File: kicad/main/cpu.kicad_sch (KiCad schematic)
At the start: 13 parts, among them SW1 SW_Push, U1 MC68030RC_PGA, U2 74HC74, U7 CY62256-70PC, Y1 CXO_DIP8

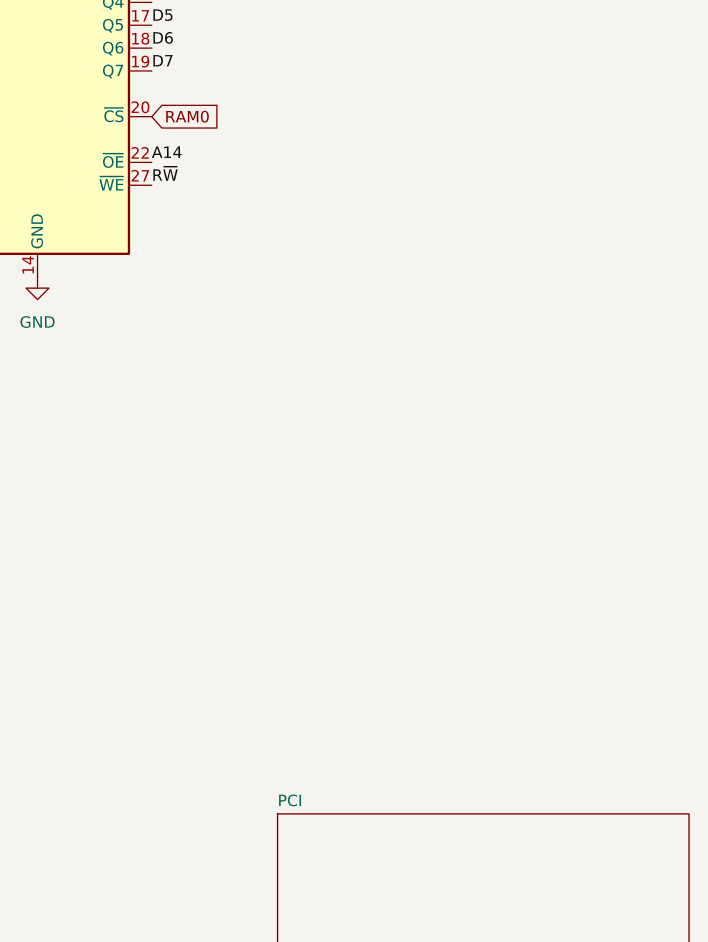
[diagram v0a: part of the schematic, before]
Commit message: rename az030 unix to az/ux
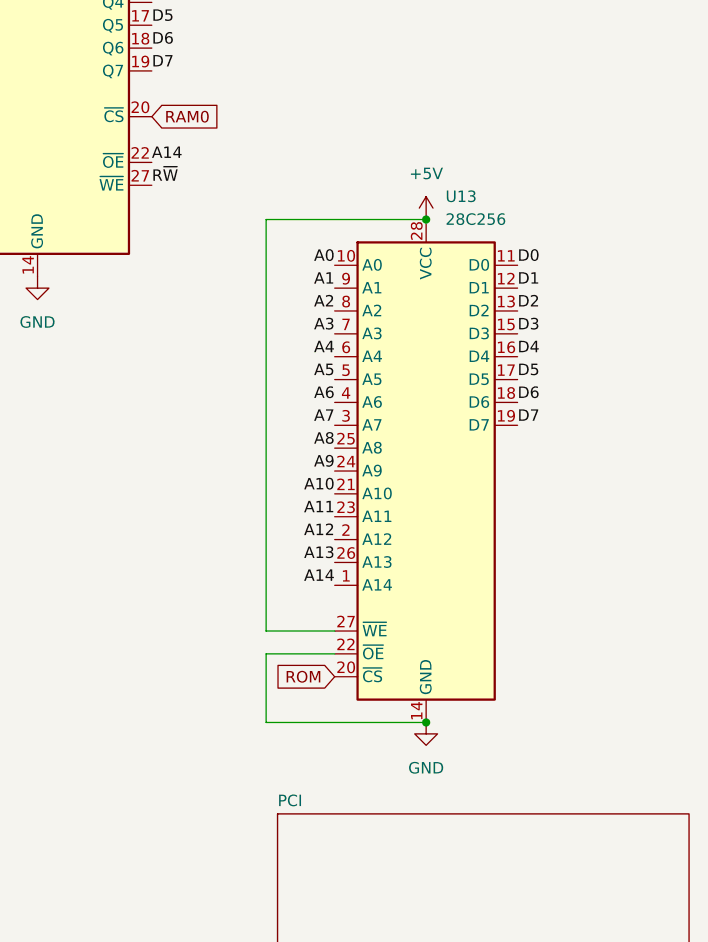
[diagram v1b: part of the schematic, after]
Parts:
- added U13: 28C256, Package_DIP:DIP-28_W15.24mm_LongPads, symbol Memory_EEPROM:28C256
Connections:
- net +5V: now also U13.27 (~{WE}), U13.28 (VCC)
- net A0: now also U13.10 (A0)
- net A1: now also U13.9 (A1)
- net A10: now also U13.21 (A10)
- net A11: now also U13.23 (A11)
- net A12: now also U13.2 (A12)
- net A13: now also U13.26 (A13)
- net A14: now also U13.1 (A14)
- net A2: now also U13.8 (A2)
- net A3: now also U13.7 (A3)
- net A4: now also U13.6 (A4)
- net A5: now also U13.5 (A5)
- net A6: now also U13.4 (A6)
- net A7: now also U13.3 (A7)
- net A8: now also U13.25 (A8)
- net A9: now also U13.24 (A9)
- net D0: now also U13.11 (D0)
- net D1: now also U13.12 (D1)
- net D2: now also U13.13 (D2)
- net D3: now also U13.15 (D3)
- net D4: now also U13.16 (D4)
- net D5: now also U13.17 (D5)
- net D6: now also U13.18 (D6)
- net D7: now also U13.19 (D7)
- net GND: now also U13.14 (GND), U13.22 (~{OE})
- new net ROM: U13.20 (~{CS})
